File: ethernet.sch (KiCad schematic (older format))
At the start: 44 parts, among them U11 KSZ9031RNXCA, Y1 ABM8G-25.000MHZ-18-D2Y-T

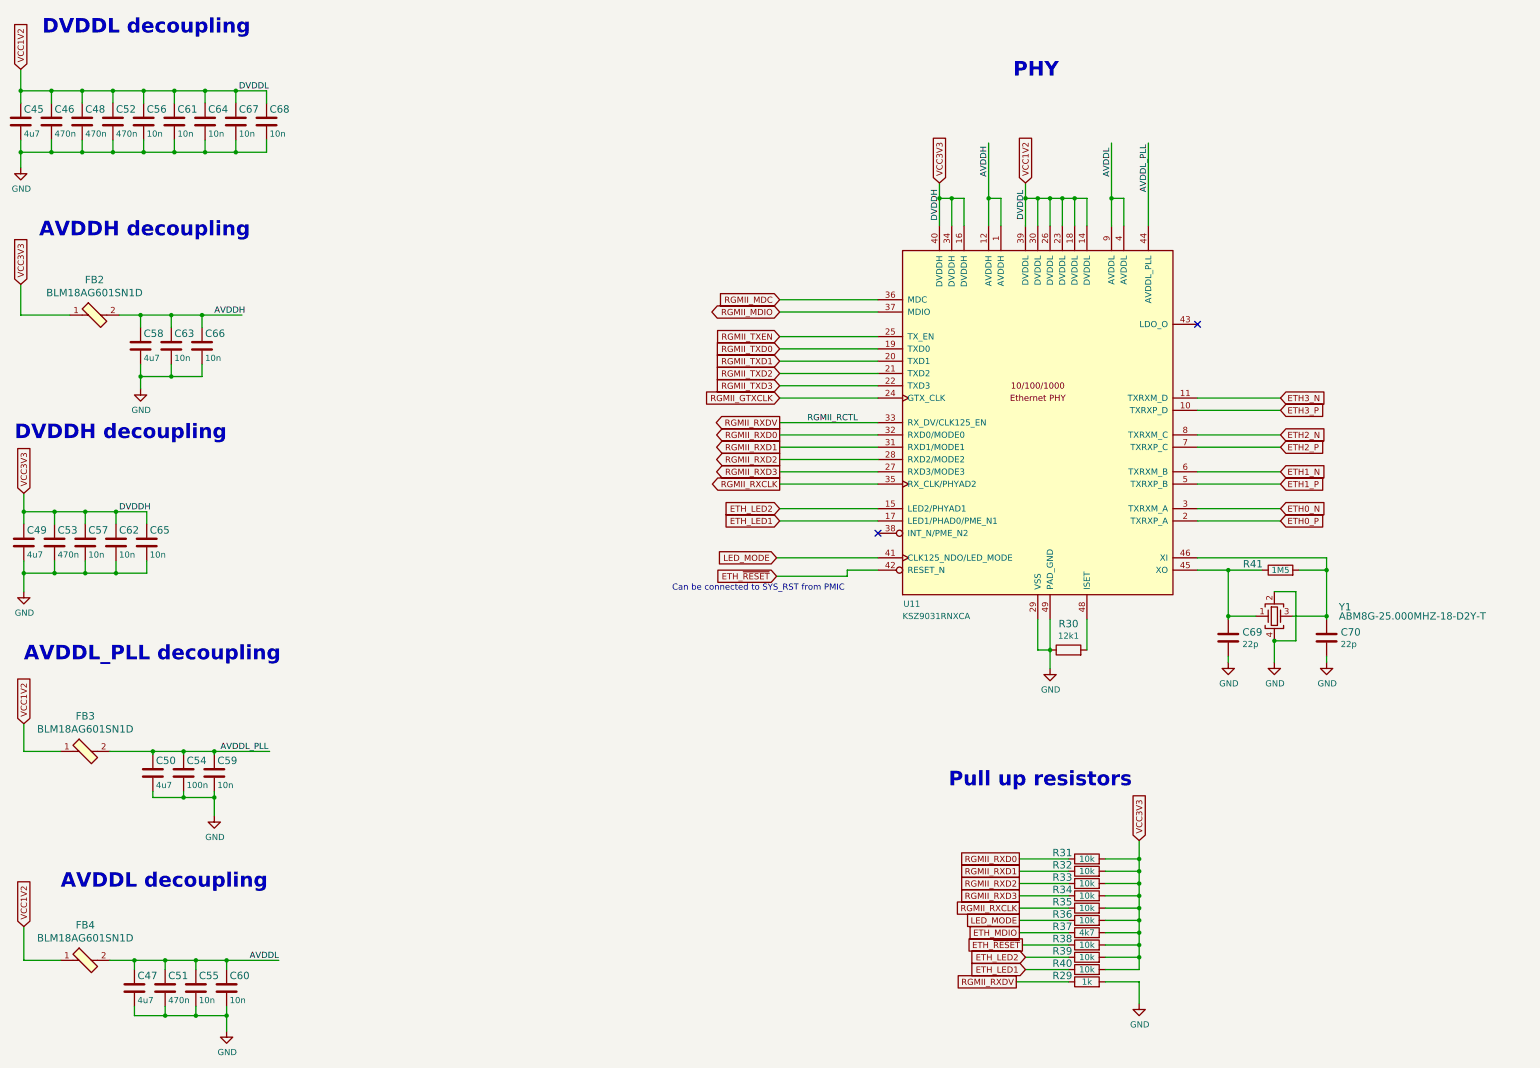
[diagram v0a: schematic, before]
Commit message: Fixed power labels on ETH
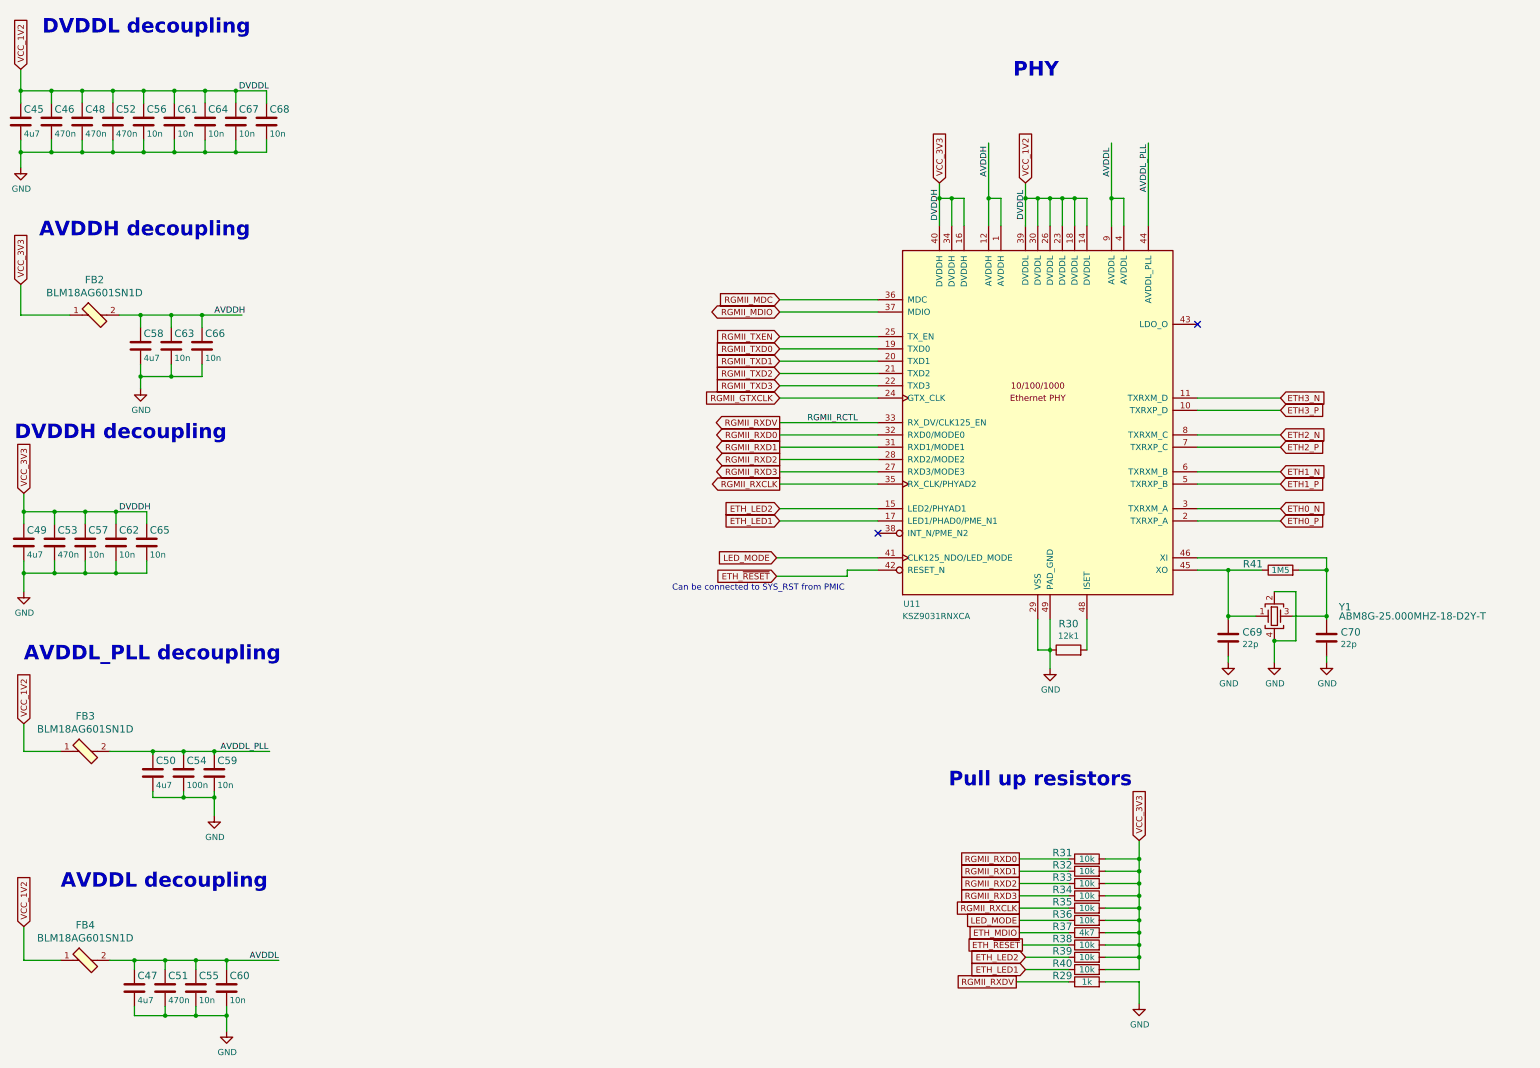
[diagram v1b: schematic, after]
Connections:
- net VCC1V2 renamed VCC_1V2
- net VCC3V3 renamed VCC_3V3
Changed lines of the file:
@@
 RGMII_RXCLK
 Text GLabel 10825 8000 1    50   Input ~ 0
-VCC3V3
+VCC_3V3
 Text GLabel 9850 8650 0    50   UnSpc ~ 0
 LED_MODE
@@
 	3150 8975 3150 9050
 Text GLabel 1750 8700 1    50   Input ~ 0
-VCC1V2
+VCC_1V2
 Wire Wire Line
 	3400 9425 3400 9350
@@
 	3475 2400 3225 2400
 Text GLabel 1725 1725 1    50   Input ~ 0
-VCC1V2
+VCC_1V2
 Wire Wire Line
 	9700 3000 9700 2775
@@
 	1725 2400 1725 2525
 Text GLabel 1750 5175 1    50   Input ~ 0
-VCC3V3
+VCC_3V3
 Text GLabel 1725 3475 1    50   Input ~ 0
-VCC3V3
+VCC_3V3
 Wire Wire Line
 	2700 4225 2950 4225
@@
 DVDDH decoupling
 Text GLabel 9200 2650 1    50   Input ~ 0
-VCC3V3
+VCC_3V3
 Wire Wire Line
 	9200 2650 9200 2775
@@
 DVDDL decoupling
 Text GLabel 9900 2650 1    50   Input ~ 0
-VCC1V2
+VCC_1V2
 Wire Wire Line
 	9900 2650 9900 2775
@@
 AVDDL_PLL decoupling
 Text GLabel 1750 7050 1    50   Input ~ 0
-VCC1V2
+VCC_1V2
 Wire Wire Line
 	3050 7275 3300 7275
